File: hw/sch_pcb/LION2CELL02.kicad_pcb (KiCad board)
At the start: 2 copper layers, 80.8 x 60.5 mm, 104 parts, among them J1 USBC_USB4105-GF-A, J10 HEADER_2x01_PARALLEL, J11 HEADER_1x02, J12 HEADER_2x05_PARALLEL, J2 CONN1_1, J3 CONN1_1, J4 JUMP_4X2, J5 HEADER_2x03_PARALLEL, J6 HEADER_2x01_PARALLEL, J7 HEADER_2x01_PARALLEL, J8 CONN1_1, J9 CONN1_1, Q1 DMT31M7LPS, Q2 AP2305AGN-HF-3, Q3 DMT31M7LPS, Q5 DMT31M7LPS, SW1 SW_Push, SW2 SW_Push, U1 BQ25792RQMR1, U2 LMR14050, U3 BQ40z50-R2

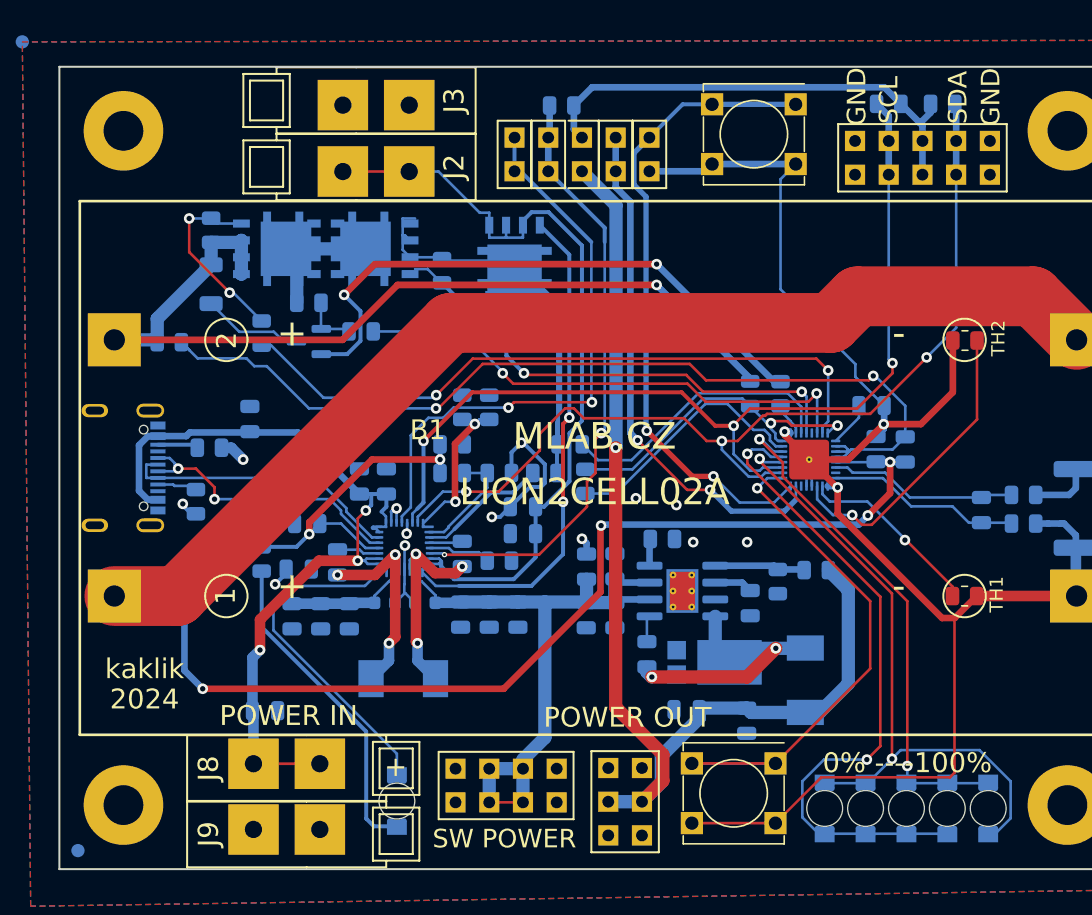
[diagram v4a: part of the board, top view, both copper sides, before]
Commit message: Uniforming track width Cleanup layout. Fix high-current paths Create copper-pours to high-current areas.
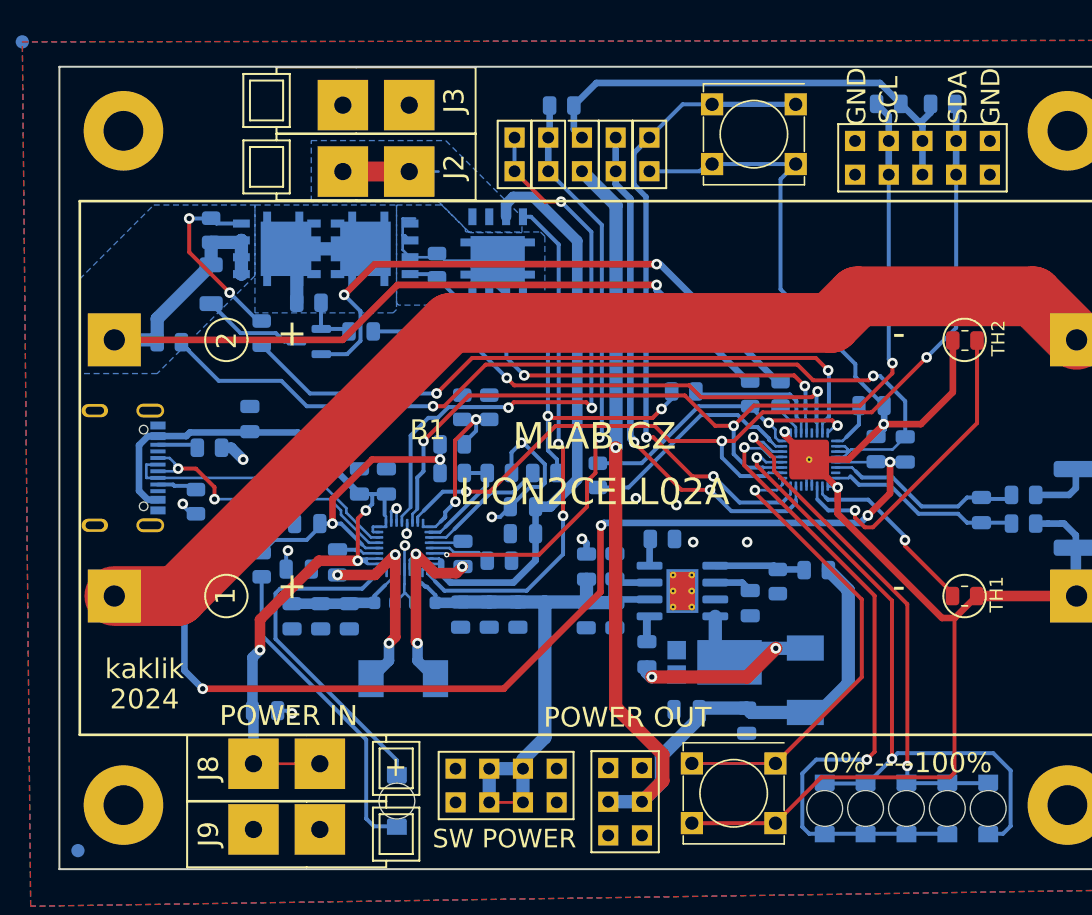
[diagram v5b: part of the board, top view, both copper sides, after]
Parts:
- moved R24 9.44 mm to (155.2, 99.2)
- moved Q1 1.42 mm to (141.1, 88.7)
- moved TH4 1.05 mm to (148.7, 105.6)
- moved R23 0.54 mm to (136.6, 89.8)
- moved R7 0.43 mm to (123.4, 112.3)
- moved C10 0.05 mm to (138.5, 111.5)
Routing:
- net Net-(U3-PACK): track 21.5 -> 10.2 mm
- net Net-(U1-nQON): track 43.7 -> 52.6 mm, vias 2 -> 3
- net /Power Input/Power_load: track 60.2 -> 52.0 mm
- net /Fuel Gauge/PACK+: track 46.8 -> 41.1 mm, vias 0 -> 2
- net Net-(Q1-G): track 37.9 -> 40.6 mm
- net /Power Input/REGN: track 28.5 -> 26.4 mm
- net Net-(U3-PTC): track 19.2 -> 17.4 mm
- net GND: track 30.7 -> 32.5 mm, vias 13 -> 14
- net VBUS: track 67.4 -> 69.1 mm
- net /Fuel Gauge/BAT: track 25.1 -> 23.5 mm
- net Net-(D1-K): track 49.9 -> 51.0 mm
- net /Fuel Gauge/SDA: track 72.7 -> 71.6 mm
- net Net-(D1-A): track 49.0 -> 50.1 mm
- net Net-(U1-TS): track 14.7 -> 13.7 mm
- net Net-(D5-K): track 38.8 -> 39.6 mm
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- added copper zone on B.Cu, net /Fuel Gauge/B+
- added copper zone on B.Cu, net /Fuel Gauge/PACK+
- added copper zone on B.Cu, net /Fuel Gauge/VCOM
- added copper zone on B.Cu, net /Power Input/Power_load

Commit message: Correct positioning of FIDUs Fix silkscreen texts.
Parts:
- moved FID3 18.1 mm to (181.1, 121.1)
- moved FID4 16.4 mm to (119.4, 81.3)
- moved FID2 12.5 mm to (183.5, 88.0)
- moved FID1 10.4 mm to (116.2, 125.8)
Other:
- board text added: "0%----100%"
- board text added: "Vcc"
- board text removed: "0% ----100%"
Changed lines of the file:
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@@
 		(at 148.5 105)
 		(property "Reference" "B1"
-			(at -12.6365 -2.8575 0)
+			(at -18.2626 -0.254 0)
 			(layer "F.SilkS")
 			(effects
@@
 	(footprint "Fiducial:Fiducial_1mm_Mask2mm"
 		(layer "B.Cu")
-		(at 105.32 72.897 180)
+		(at 119.417 81.3272 180)
 		(descr "Circular Fiducial, 1mm bare copper, 2mm soldermask opening (Level A)")
 		(tags "fiducial")
@@
 	(footprint "Fiducial:Fiducial_1mm_Mask2mm"
 		(layer "B.Cu")
-		(at 109.511 133.829 180)
+		(at 116.1658 125.7772 180)
 		(descr "Circular Fiducial, 1mm bare copper, 2mm soldermask opening (Level A)")
 		(tags "fiducial")
@@
 	(footprint "Fiducial:Fiducial_1mm_Mask2mm"
 		(layer "B.Cu")
-		(at 187.489 76.171 180)
+		(at 183.4758 87.9566 180)
 		(descr "Circular Fiducial, 1mm bare copper, 2mm soldermask opening (Level A)")
 		(tags "fiducial")
@@
 	(footprint "Fiducial:Fiducial_1mm_Mask2mm"
 		(layer "B.Cu")
-		(at 190.283 136.623 180)
+		(at 181.139 121.0528 180)
 		(descr "Circular Fiducial, 1mm bare copper, 2mm soldermask opening (Level A)")
 		(tags "fiducial")
@@
 		)
 	)
+	(gr_text "Vcc"
+		(at 173.138 79.092 90)
+		(layer "F.SilkS")
+		(effects
+			(font
+				(size 1.4 1.4)
+				(thickness 0.3)
+			)
+			(justify left)
+		)
+	)
 	(gr_text "GND"
 		(at 168.185 79.219 90)
@@
 		)
 	)
-	(gr_text "0% ----100%"
+	(gr_text "0%----100%"
 		(at 171.995 127.225 0)
 		(layer "F.SilkS")
@@
 		(start 130.593 111.98646)
 		(end 130.588525 111.990935)
-		(width 0.3)
+		(width 0.8)
 		(layer "F.Cu")
 		(net 5)
@@
 		(start 131.198 108.206)
 		(end 130.593 108.81)
-		(width 0.3)
+		(width 0.8)
 		(layer "F.Cu")
 		(net 5)
@@
 		(start 130.593 108.81)
 		(end 130.593 111.98646)
-		(width 0.3)
+		(width 0.8)
 		(layer "F.Cu")
 		(net 5)
@@
 	)
 	(zone
-		(net 37)
-		(net_name "/Fuel Gauge/VCOM")
-		(layer "B.Cu")
-		(hatch edge 0.5)
-		(priority 2)
-		(connect_pads yes
-			(clearance 0.5)
-		)
-		(min_thickness 0.25)
-		(filled_areas_thickness no)
-		(fill yes
-			(thermal_gap 0.5)
-			(thermal_bridge_width 0.5)
-		)
-		(polygon
-			(pts
-				(xy 122.846 85.188) (xy 133.514 85.188) (xy 133.514 93.062) (xy 133.26 93.316) (xy 122.846 93.316)
-			)
-		)
-	)
-	(zone
 		(net 39)
 		(net_name "Net-(Q5-G)")
@@
 		(name "$teardrop_padvia$")
 		(hatch full 0.1)
-		(priority 30000)
+		(priority 30001)
 		(attr
 			(teardrop
@@
 	)
 	(zone
-		(net 12)
-		(net_name "/Fuel Gauge/PACK+")
+		(net 37)
+		(net_name "/Fuel Gauge/VCOM")
 		(layer "B.Cu")
 		(hatch edge 0.5)
-		(priority 3)
+		(priority 2)
 		(connect_pads yes
 			(clearance 0.5)
@@
 		(polygon
 			(pts
-				(xy 133.514 85.188) (xy 136.9176 85.188) (xy 138.6956 86.966) (xy 138.6956 87.1692) (xy 138.7464 87.22)
-				(xy 144.3598 87.22) (xy 144.69 87.5502) (xy 144.69 92.7318) (xy 133.6664 92.7318) (xy 133.514 92.5794)
+				(xy 122.846 85.188) (xy 133.514 85.188) (xy 133.514 93.062) (xy 133.26 93.316) (xy 122.846 93.316)
 			)
 		)
 	)
 	(zone
-		(net 38)
-		(net_name "Net-(Q3-G)")
+		(net 34)
+		(net_name "Net-(Q1-G)")
 		(layer "B.Cu")
 		(name "$teardrop_padvia$")
 		(hatch full 0.1)
-		(priority 30001)
+		(priority 30002)
 		(attr
 			(teardrop
@@
 		(polygon
 			(pts
-				(xy 120.886999 86.435) (xy 120.886999 86.735) (xy 121.191999 86.89) (xy 121.827999 86.585) (xy 121.191999 86.28)
+				(xy 143.54147 86.1836) (xy 143.753601 85.971469) (xy 143.344 85.770413) (xy 143.038293 86.073292)
+				(xy 143.344 86.380428)
+			)
+		)
+	)
+	(zone
+		(net 12)
+		(net_name "/Fuel Gauge/PACK+")
+		(layer "B.Cu")
+		(hatch edge 0.5)
+		(priority 3)
+		(connect_pads yes
+			(clearance 0.5)
+		)
+		(min_thickness 0.25)
+		(filled_areas_thickness no)
+		(fill yes
+			(thermal_gap 0.5)
+			(thermal_bridge_width 0.5)
+		)
+		(polygon
+			(pts
+				(xy 133.514 85.188) (xy 136.9176 85.188) (xy 138.6956 86.966) (xy 138.6956 87.1692) (xy 138.7464 87.22)
+				(xy 144.3598 87.22) (xy 144.69 87.5502) (xy 144.69 92.7318) (xy 133.6664 92.7318) (xy 133.514 92.5794)
 			)
 		)
@@
 	)
 	(zone
-		(net 34)
-		(net_name "Net-(Q1-G)")
+		(net 38)
+		(net_name "Net-(Q3-G)")
 		(layer "B.Cu")
 		(name "$teardrop_padvia$")
 		(hatch full 0.1)
-		(priority 30002)
+		(priority 30000)
 		(attr
 			(teardrop
@@
 		(polygon
 			(pts
-				(xy 143.54147 86.1836) (xy 143.753601 85.971469) (xy 143.344 85.770413) (xy 143.038293 86.073292)
-				(xy 143.344 86.380428)
+				(xy 120.886999 86.435) (xy 120.886999 86.735) (xy 121.191999 86.89) (xy 121.827999 86.585) (xy 121.191999 86.28)
 			)
 		)

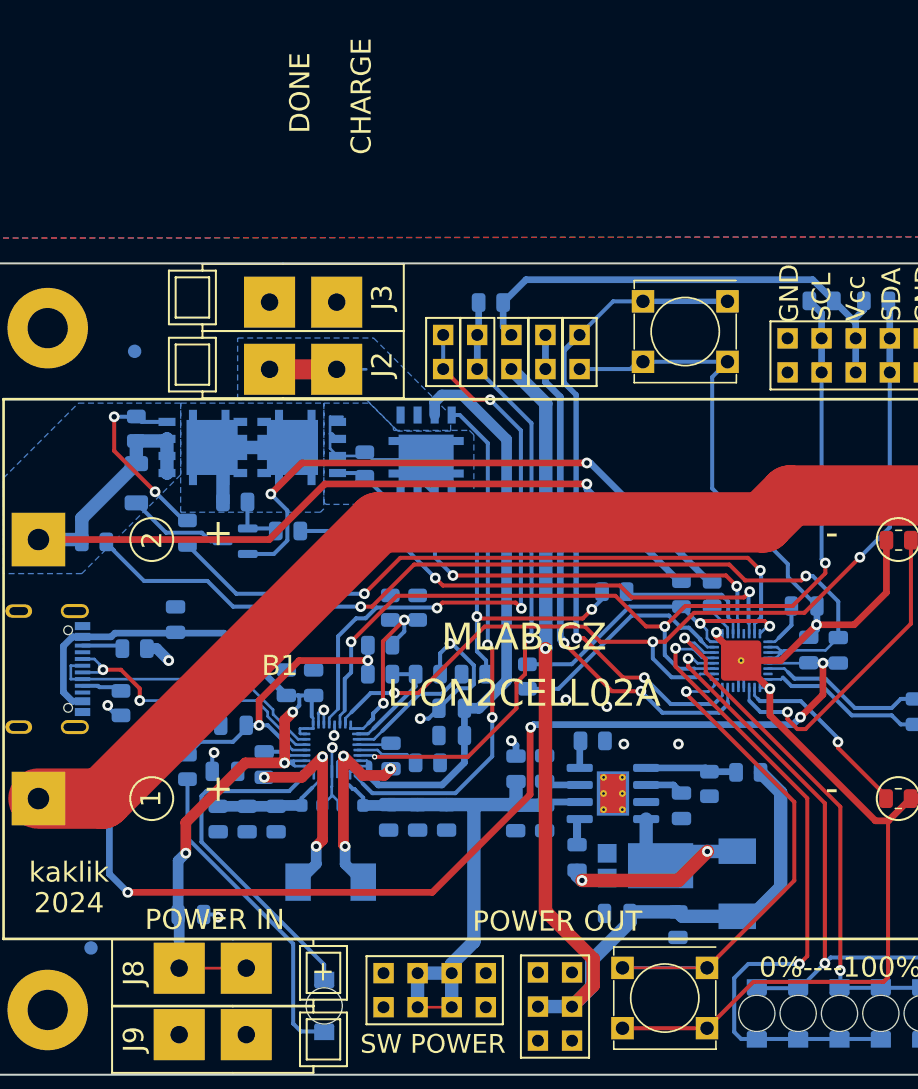
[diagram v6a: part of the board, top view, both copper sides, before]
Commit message: USB data lines layout improvement. Zones definitions for improving noise imunity.
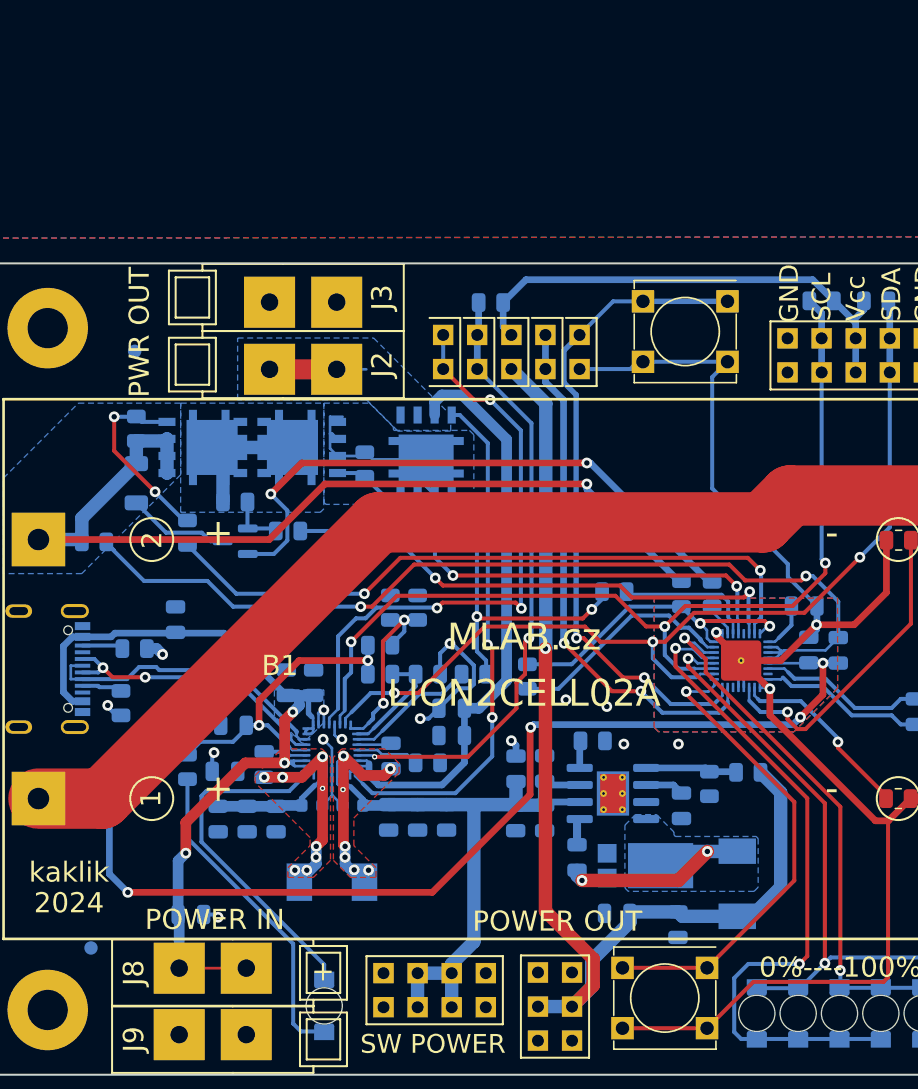
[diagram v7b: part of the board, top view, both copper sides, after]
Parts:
- J10, J11, J6, J7: footprint Mlab_Pin_Headers:Straight_1x02 -> Mlab_Pin_Headers:Straight_2x01
- Q1, Q3, Q5: value DMT31M7LPS -> DMTH3002LPS
- moved L1 0.09 mm to (134.1, 120.9)
- turned J10 to 90 degrees
- turned J11 to 90 degrees
- turned J6 to 90 degrees
- turned J7 to 90 degrees
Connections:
- J11 pad 1: Net-(U3-~{PRES/SHDWN}) -> GND1
- J11 pad 2: GND1 -> Net-(U3-~{PRES/SHDWN})
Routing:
- net Net-(U1-SW1): track 16.3 -> 19.1 mm, vias 3 -> 8
- net Net-(D2-K): track 18.2 -> 15.8 mm
- net /Power Input/System_load: track 49.0 -> 46.7 mm
- net Net-(U1-PMID): track 9.28 -> 11.2 mm
- net Net-(U1-SW2): track 15.7 -> 17.2 mm, vias 3 -> 7
- net /Power Input/D+: track 22.6 -> 21.4 mm
- net GND: track 32.5 -> 33.3 mm
- net /Power Input/D-: track 21.5 -> 22.2 mm
- added copper zone on B.Cu, net GND1
- added copper zone on F.Cu, net GND1
- added copper zone on B.Cu, net Net-(D2-K)
- added copper zone on F.Cu, net Net-(U1-SW1)
- added copper zone on F.Cu, net Net-(U1-SW2)
- added copper zone on B.Cu, net VBUS
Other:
- board text added: "MLAB.cz"
- board text added: "PWR OUT"
- board text removed: "CHARGE"
- board text removed: "DONE"
